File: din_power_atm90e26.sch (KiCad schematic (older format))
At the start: 60 parts, among them J1 CONN_01X06, J2 VBAT, J3 CONN_01X08, J4 CONN_02X18, J5 CONN_01X08, U1 MCP73831-2-OT, U2 TLV1117-33, U3 TLV1117-33, U4 Hi-Link_SMPS, U5 dc-dc

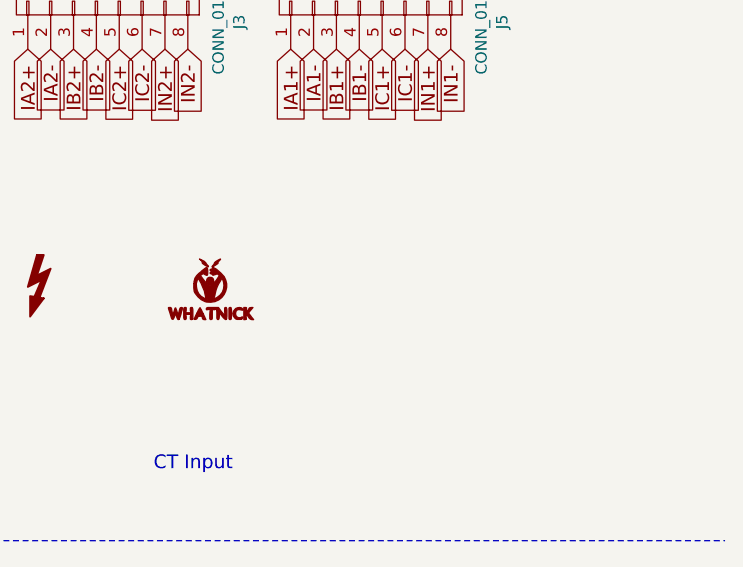
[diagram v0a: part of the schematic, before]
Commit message: Add OSHW logo
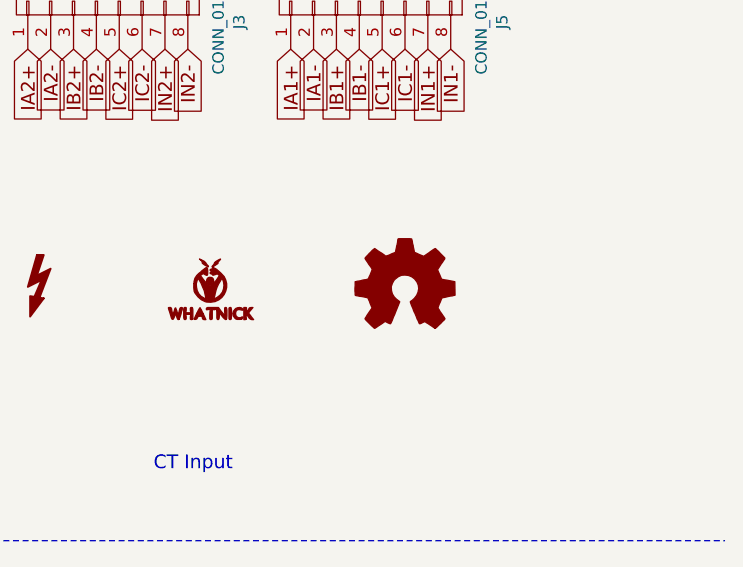
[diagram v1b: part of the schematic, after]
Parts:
- added LOGO_OSHW1: Logo_Open_Hardware_Small, Symbols:OSHW-Symbol_6.7x6mm_SilkScreen, symbol Logo_Open_Hardware_Small
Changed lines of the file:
@@
 EESchema Schematic File Version 2
+LIBS:graphic_symbols
 LIBS:power
 LIBS:device
@@
 	1    0    0    -1
 $EndComp
+$Comp
+L Logo_Open_Hardware_Small LOGO_OSHW1
+U 1 1 5A0F959B
+P 9850 2600
+F 0 "LOGO_OSHW1" H 9850 2875 50  0001 C CNN
+F 1 "Logo_Open_Hardware_Small" H 9850 2375 50  0001 C CNN
+F 2 "Symbols:OSHW-Symbol_6.7x6mm_SilkScreen" H 9850 2600 50  0001 C CNN
+F 3 "" H 9850 2600 50  0001 C CNN
+	1    9850 2600
+	1    0    0    -1
+$EndComp

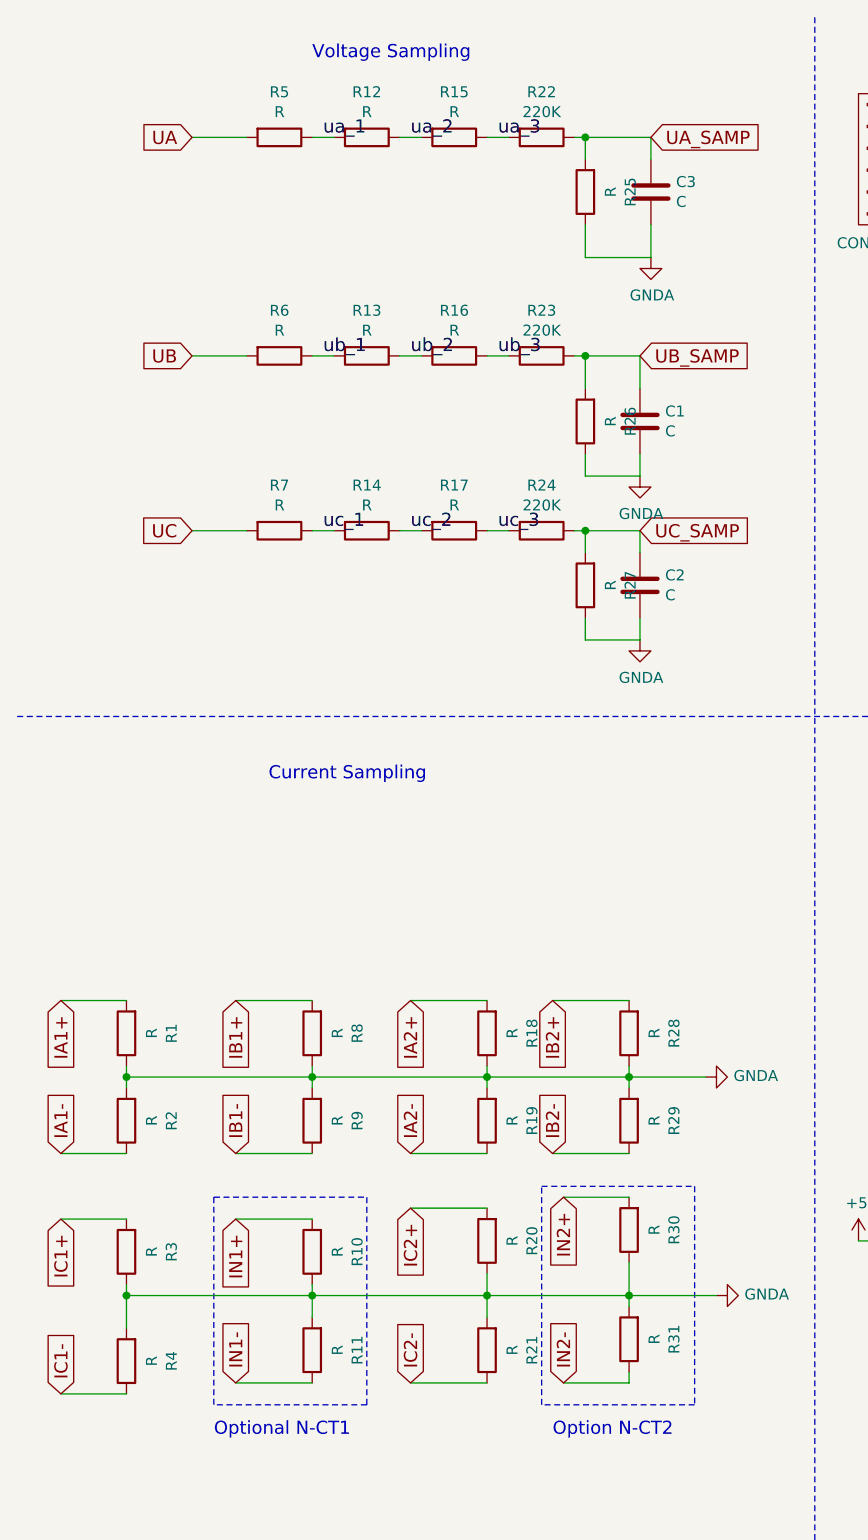
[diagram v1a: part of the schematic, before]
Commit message: Add more part numbers
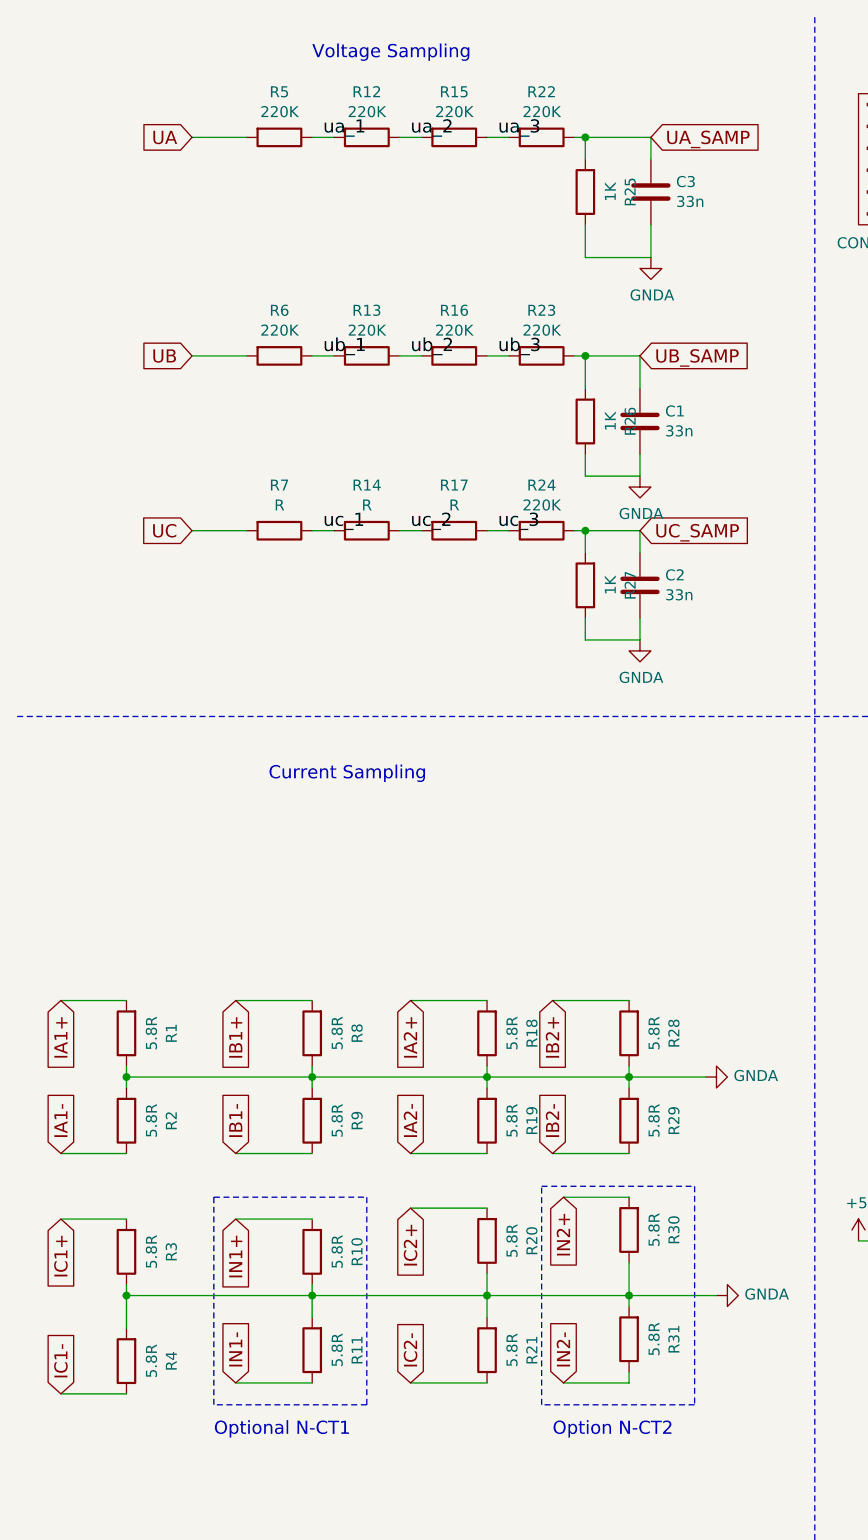
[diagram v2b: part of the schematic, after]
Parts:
- C1, C2, C3: value C -> 33n
- R1, R10, R11, R18, R19, R2, R20, R21, R28, R29, R3, R30, R31, R4, R8, R9: value R -> 5.8R
- R12, R13, R15, R16, R6: value R -> 220K
- R25: value R -> 1K; manf# (none) -> CRG0603F1K0
- R26, R27: value R -> 1K
- R5: value R -> 220K; manf# (none) -> CRG1206F220K
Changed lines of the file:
@@
 P 1650 1050
 F 0 "R5" V 1443 1050 50  0000 C CNN
-F 1 "R" V 1534 1050 50  0000 C CNN
+F 1 "220K" V 1534 1050 50  0000 C CNN
 F 2 "Resistors_SMD:R_1206" V 1580 1050 50  0001 C CNN
 F 3 "" H 1650 1050 50  0001 C CNN
+F 4 "CRG1206F220K" H 1650 1050 60  0001 C CNN "manf#"
 	1    1650 1050
 	0    1    1    0
@@
 P 2050 1050
 F 0 "R12" V 1843 1050 50  0000 C CNN
-F 1 "R" V 1934 1050 50  0000 C CNN
+F 1 "220K" V 1934 1050 50  0000 C CNN
 F 2 "Resistors_SMD:R_1206" V 1980 1050 50  0001 C CNN
 F 3 "" H 2050 1050 50  0001 C CNN
@@
 P 2450 1050
 F 0 "R15" V 2243 1050 50  0000 C CNN
-F 1 "R" V 2334 1050 50  0000 C CNN
+F 1 "220K" V 2334 1050 50  0000 C CNN
 F 2 "Resistors_SMD:R_1206" V 2380 1050 50  0001 C CNN
 F 3 "" H 2450 1050 50  0001 C CNN
@@
 P 1650 2050
 F 0 "R6" V 1443 2050 50  0000 C CNN
-F 1 "R" V 1534 2050 50  0000 C CNN
+F 1 "220K" V 1534 2050 50  0000 C CNN
 F 2 "Resistors_SMD:R_1206" V 1580 2050 50  0001 C CNN
 F 3 "" H 1650 2050 50  0001 C CNN
@@
 P 2050 2050
 F 0 "R13" V 1843 2050 50  0000 C CNN
-F 1 "R" V 1934 2050 50  0000 C CNN
+F 1 "220K" V 1934 2050 50  0000 C CNN
 F 2 "Resistors_SMD:R_1206" V 1980 2050 50  0001 C CNN
 F 3 "" H 2050 2050 50  0001 C CNN
@@
 P 2450 2050
 F 0 "R16" V 2243 2050 50  0000 C CNN
-F 1 "R" V 2334 2050 50  0000 C CNN
+F 1 "220K" V 2334 2050 50  0000 C CNN
 F 2 "Resistors_SMD:R_1206" V 2380 2050 50  0001 C CNN
 F 3 "" H 2450 2050 50  0001 C CNN
@@
 P 3050 1300
 F 0 "R25" V 2843 1300 50  0000 C CNN
-F 1 "R" V 2934 1300 50  0000 C CNN
+F 1 "1K" V 2934 1300 50  0000 C CNN
 F 2 "Resistors_SMD:R_0603" V 2980 1300 50  0001 C CNN
 F 3 "" H 3050 1300 50  0001 C CNN
+F 4 "CRG0603F1K0" H 3050 1300 60  0001 C CNN "manf#"
 	1    3050 1300
 	-1   0    0    1
@@
 P 3050 2350
 F 0 "R26" V 2843 2350 50  0000 C CNN
-F 1 "R" V 2934 2350 50  0000 C CNN
+F 1 "1K" V 2934 2350 50  0000 C CNN
 F 2 "Resistors_SMD:R_0603" V 2980 2350 50  0001 C CNN
 F 3 "" H 3050 2350 50  0001 C CNN
@@
 P 3050 3100
 F 0 "R27" V 2843 3100 50  0000 C CNN
-F 1 "R" V 2934 3100 50  0000 C CNN
+F 1 "1K" V 2934 3100 50  0000 C CNN
 F 2 "Resistors_SMD:R_0603" V 2980 3100 50  0001 C CNN
 F 3 "" H 3050 3100 50  0001 C CNN
@@
 P 3350 1300
 F 0 "C3" H 3465 1346 50  0000 L CNN
-F 1 "C" H 3465 1255 50  0000 L CNN
+F 1 "33n" H 3465 1255 50  0000 L CNN
 F 2 "Capacitors_SMD:C_0603" H 3388 1150 50  0001 C CNN
 F 3 "" H 3350 1300 50  0001 C CNN
@@
 P 3300 2350
 F 0 "C1" H 3415 2396 50  0000 L CNN
-F 1 "C" H 3415 2305 50  0000 L CNN
+F 1 "33n" H 3415 2305 50  0000 L CNN
 F 2 "Capacitors_SMD:C_0603" H 3338 2200 50  0001 C CNN
 F 3 "" H 3300 2350 50  0001 C CNN
@@
 P 3300 3100
 F 0 "C2" H 3415 3146 50  0000 L CNN
-F 1 "C" H 3415 3055 50  0000 L CNN
+F 1 "33n" H 3415 3055 50  0000 L CNN
 F 2 "Capacitors_SMD:C_0603" H 3338 2950 50  0001 C CNN
 F 3 "" H 3300 3100 50  0001 C CNN
@@
 P 950 5150
 F 0 "R1" V 743 5150 50  0000 C CNN
-F 1 "R" V 834 5150 50  0000 C CNN
+F 1 "5.8R" V 834 5150 50  0000 C CNN
 F 2 "Resistors_SMD:R_0603" V 880 5150 50  0001 C CNN
 F 3 "" H 950 5150 50  0001 C CNN
@@
 P 950 5550
 F 0 "R2" V 743 5550 50  0000 C CNN
-F 1 "R" V 834 5550 50  0000 C CNN
+F 1 "5.8R" V 834 5550 50  0000 C CNN
 F 2 "Resistors_SMD:R_0603" V 880 5550 50  0001 C CNN
 F 3 "" H 950 5550 50  0001 C CNN
@@
 P 1800 5150
 F 0 "R8" V 1593 5150 50  0000 C CNN
-F 1 "R" V 1684 5150 50  0000 C CNN
+F 1 "5.8R" V 1684 5150 50  0000 C CNN
 F 2 "Resistors_SMD:R_0603" V 1730 5150 50  0001 C CNN
 F 3 "" H 1800 5150 50  0001 C CNN
@@
 P 1800 5550
 F 0 "R9" V 1593 5550 50  0000 C CNN
-F 1 "R" V 1684 5550 50  0000 C CNN
+F 1 "5.8R" V 1684 5550 50  0000 C CNN
 F 2 "Resistors_SMD:R_0603" V 1730 5550 50  0001 C CNN
 F 3 "" H 1800 5550 50  0001 C CNN
@@
 P 2600 5150
 F 0 "R18" V 2393 5150 50  0000 C CNN
-F 1 "R" V 2484 5150 50  0000 C CNN
+F 1 "5.8R" V 2484 5150 50  0000 C CNN
 F 2 "Resistors_SMD:R_0603" V 2530 5150 50  0001 C CNN
 F 3 "" H 2600 5150 50  0001 C CNN
@@
 P 2600 5550
 F 0 "R19" V 2393 5550 50  0000 C CNN
-F 1 "R" V 2484 5550 50  0000 C CNN
+F 1 "5.8R" V 2484 5550 50  0000 C CNN
 F 2 "Resistors_SMD:R_0603" V 2530 5550 50  0001 C CNN
 F 3 "" H 2600 5550 50  0001 C CNN
@@
 P 3250 5150
 F 0 "R28" V 3043 5150 50  0000 C CNN
-F 1 "R" V 3134 5150 50  0000 C CNN
+F 1 "5.8R" V 3134 5150 50  0000 C CNN
 F 2 "Resistors_SMD:R_0603" V 3180 5150 50  0001 C CNN
 F 3 "" H 3250 5150 50  0001 C CNN
@@
 P 3250 5550
 F 0 "R29" V 3043 5550 50  0000 C CNN
-F 1 "R" V 3134 5550 50  0000 C CNN
+F 1 "5.8R" V 3134 5550 50  0000 C CNN
 F 2 "Resistors_SMD:R_0603" V 3180 5550 50  0001 C CNN
 F 3 "" H 3250 5550 50  0001 C CNN
@@
 P 950 6150
 F 0 "R3" V 743 6150 50  0000 C CNN
-F 1 "R" V 834 6150 50  0000 C CNN
+F 1 "5.8R" V 834 6150 50  0000 C CNN
 F 2 "Resistors_SMD:R_0603" V 880 6150 50  0001 C CNN
 F 3 "" H 950 6150 50  0001 C CNN
@@
 P 950 6650
 F 0 "R4" V 743 6650 50  0000 C CNN
-F 1 "R" V 834 6650 50  0000 C CNN
+F 1 "5.8R" V 834 6650 50  0000 C CNN
 F 2 "Resistors_SMD:R_0603" V 880 6650 50  0001 C CNN
 F 3 "" H 950 6650 50  0001 C CNN
@@
 P 1800 6150
 F 0 "R10" V 1593 6150 50  0000 C CNN
-F 1 "R" V 1684 6150 50  0000 C CNN
+F 1 "5.8R" V 1684 6150 50  0000 C CNN
 F 2 "Resistors_SMD:R_0603" V 1730 6150 50  0001 C CNN
 F 3 "" H 1800 6150 50  0001 C CNN
@@
 P 1800 6600
 F 0 "R11" V 1593 6600 50  0000 C CNN
-F 1 "R" V 1684 6600 50  0000 C CNN
+F 1 "5.8R" V 1684 6600 50  0000 C CNN
 F 2 "Resistors_SMD:R_0603" V 1730 6600 50  0001 C CNN
 F 3 "" H 1800 6600 50  0001 C CNN
@@
 P 2600 6100
 F 0 "R20" V 2393 6100 50  0000 C CNN
-F 1 "R" V 2484 6100 50  0000 C CNN
+F 1 "5.8R" V 2484 6100 50  0000 C CNN
 F 2 "Resistors_SMD:R_0603" V 2530 6100 50  0001 C CNN
 F 3 "" H 2600 6100 50  0001 C CNN
@@
 P 2600 6600
 F 0 "R21" V 2393 6600 50  0000 C CNN
-F 1 "R" V 2484 6600 50  0000 C CNN
+F 1 "5.8R" V 2484 6600 50  0000 C CNN
 F 2 "Resistors_SMD:R_0603" V 2530 6600 50  0001 C CNN
 F 3 "" H 2600 6600 50  0001 C CNN
@@
 P 3250 6050
 F 0 "R30" V 3043 6050 50  0000 C CNN
-F 1 "R" V 3134 6050 50  0000 C CNN
+F 1 "5.8R" V 3134 6050 50  0000 C CNN
 F 2 "Resistors_SMD:R_0603" V 3180 6050 50  0001 C CNN
 F 3 "" H 3250 6050 50  0001 C CNN
@@
 P 3250 6550
 F 0 "R31" V 3043 6550 50  0000 C CNN
-F 1 "R" V 3134 6550 50  0000 C CNN
+F 1 "5.8R" V 3134 6550 50  0000 C CNN
 F 2 "Resistors_SMD:R_0603" V 3180 6550 50  0001 C CNN
 F 3 "" H 3250 6550 50  0001 C CNN

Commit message: Address issue #1 with changes to schematic component
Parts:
- C5: manf# (none) -> 0603ZD105KAT2A
- R1: manf# (none) -> CPF0603B5R76E1
- U1: manf# (none) -> MCP73831T-3ACI/OT
- U2, U3: value TLV1117-33 -> AP7365-33YG-13; symbol TLV1117-33 -> AP7365-33YG-13
- U5: manf# (none) -> ROE-0505S
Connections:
- net +3.3V_ISO: now also U3.1 (VO); no longer U3.2 (VO)
- net +3V3: now also U2.1 (VO); no longer U2.2 (VO)
- net GNDA: now also U3.2 (GND); no longer U3.1 (GND)
- net GNDPWR: now also U2.2 (GND); no longer U2.1 (GND)
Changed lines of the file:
@@
 F 2 "hi-link_smps:SIP4" H 5800 1150 60  0001 C CNN
 F 3 "" H 5800 1150 60  0001 C CNN
+F 4 "ROE-0505S" H 5800 1150 60  0001 C CNN "manf#"
 	1    5800 1150
 	1    0    0    -1
@@
 F 2 "Resistors_SMD:R_0603" V 880 5150 50  0001 C CNN
 F 3 "" H 950 5150 50  0001 C CNN
+F 4 "CPF0603B5R76E1" H 950 5150 60  0001 C CNN "manf#"
 	1    950  5150
 	-1   0    0    1
@@
 Power Systems - Battery and 3.3V
 $Comp
-L TLV1117-33 U3
+L AP7365-33YG-13 U3
 U 1 1 59F7360D
 P 5550 4050
 F 0 "U3" H 5550 4292 50  0000 C CNN
-F 1 "TLV1117-33" H 5550 4201 50  0000 C CNN
+F 1 "AP7365-33YG-13" H 5550 4201 50  0000 C CNN
 F 2 "TO_SOT_Packages_SMD:SOT-89-3" H 5550 4050 50  0001 C CNN
 F 3 "" H 5550 4050 50  0001 C CNN
@@
 $EndComp
 $Comp
-L TLV1117-33 U2
+L AP7365-33YG-13 U2
 U 1 1 59F7360E
 P 5500 5000
 F 0 "U2" H 5500 5242 50  0000 C CNN
-F 1 "TLV1117-33" H 5500 5151 50  0000 C CNN
+F 1 "AP7365-33YG-13" H 5500 5151 50  0000 C CNN
 F 2 "TO_SOT_Packages_SMD:SOT-89-3" H 5500 5000 50  0001 C CNN
 F 3 "" H 5500 5000 50  0001 C CNN
@@
 F 2 "Capacitors_SMD:C_0603" H 5138 4100 50  0001 C CNN
 F 3 "" H 5100 4250 50  0001 C CNN
+F 4 "0603ZD105KAT2A" H 5100 4250 60  0001 C CNN "manf#"
 	1    5100 4250
 	1    0    0    -1
@@
 F 2 "TO_SOT_Packages_SMD:SOT-23-5" H 5400 6200 50  0001 L CIN
 F 3 "" H 5200 6400 50  0001 C CNN
+F 4 "MCP73831T-3ACI/OT" H 5350 6450 60  0001 C CNN "manf#"
 	1    5350 6450
 	1    0    0    -1

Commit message: Add new part numbers and high voltage sym
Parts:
- added SYM1: SYM_Flash_Small, Whatnick_logo:Fsilk_HV, symbol SYM_Flash_Small
- F1: manf# F74007-000 -> 0ZRE0012FF1C
- R5: manf# CRG1206F220K -> CRCW1206220KFKEA
- RV3: manf# B72660M0251K072 -> VP3225K401R275
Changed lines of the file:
@@
 F 2 "SMD_Packages:SMD-4032" V 2180 -300 50  0001 C CNN
 F 3 "" H 2250 -300 50  0001 C CNN
-F 4 "B72660M0251K072" H 4850 1300 60  0001 C CNN "manf#"
+F 4 "VP3225K401R275" H 4850 1300 60  0001 C CNN "manf#"
 	1    4850 1300
 	0    1    1    0
@@
 F 2 "Resistors_SMD:R_1206" V 1580 1050 50  0001 C CNN
 F 3 "" H 1650 1050 50  0001 C CNN
-F 4 "CRG1206F220K" H 1650 1050 60  0001 C CNN "manf#"
+F 4 "CRCW1206220KFKEA" H 1650 1050 60  0001 C CNN "manf#"
 	1    1650 1050
 	0    1    1    0
@@
 F 2 "Capacitors_THT:C_Disc_D10.0mm_W2.5mm_P5.00mm" H 5000 2600 50  0001 L CNN
 F 3 "" H 4950 2800 50  0001 C CNN
-F 4 "F74007-000" H 4950 2800 60  0001 C CNN "manf#"
+F 4 "0ZRE0012FF1C" H 4950 2800 60  0001 C CNN "manf#"
 	1    4950 2800
 	0    1    1    0
@@
 uc_3
 $Comp
-L SYM_Flash_Small #SYM1
+L SYM_Flash_Small SYM1
 U 1 1 59F73620
 P 8250 2600
-F 0 "#SYM1" V 8160 2600 50  0001 C CNN
+F 0 "SYM1" V 8160 2600 50  0001 C CNN
 F 1 "SYM_Flash_Small" V 8340 2600 50  0001 C CNN
-F 2 "" H 8250 2575 50  0001 C CNN
+F 2 "Whatnick_logo:Fsilk_HV" H 8250 2575 50  0001 C CNN
 F 3 "" H 8650 2500 50  0001 C CNN
 	1    8250 2600
